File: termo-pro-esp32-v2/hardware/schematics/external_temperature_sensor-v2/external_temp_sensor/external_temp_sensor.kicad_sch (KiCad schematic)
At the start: 1 part

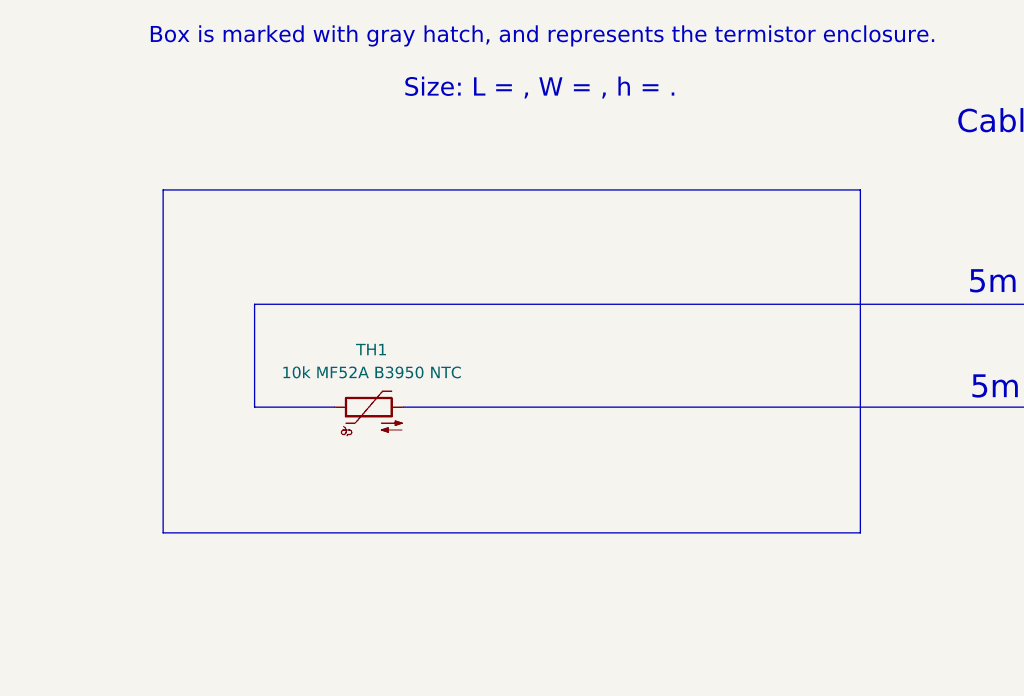
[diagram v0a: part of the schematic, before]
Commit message: Starting Unit PCB compleate.
Some footprint issues were encountered on the initial unit PCB, regarding the ceramic capacitors and the 1×02 5.08 mm screw terminal.

-In the thermostat schematic, the ceramic capacitors were updated to a disc footprint , as well in the starting unit scheme.

-Thermostat PCB is currently in progress.
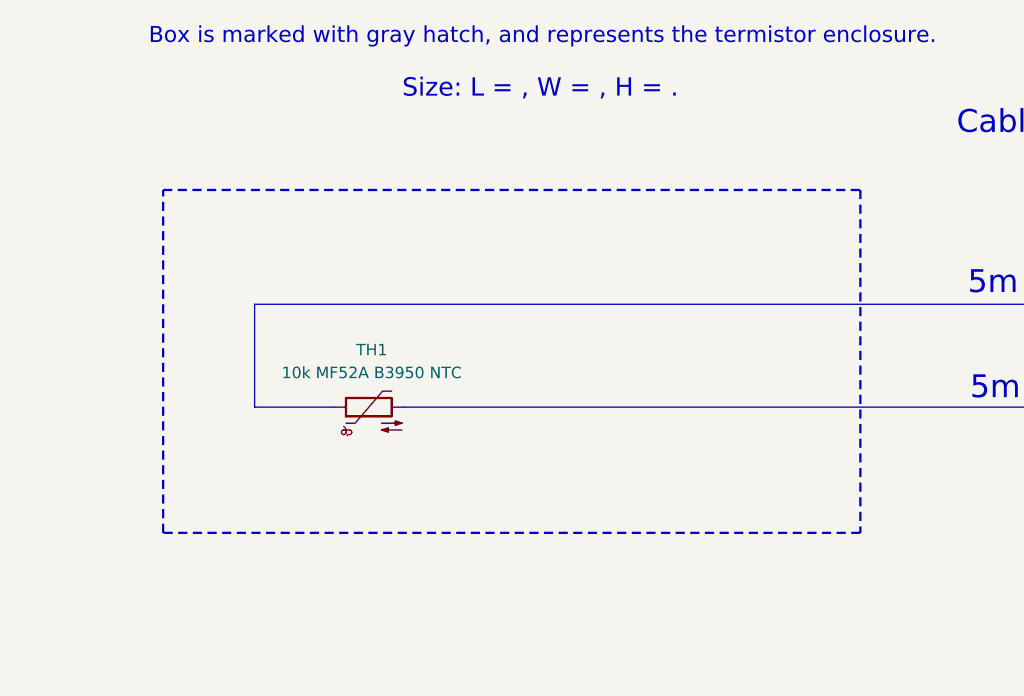
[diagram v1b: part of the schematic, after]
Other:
- note added: "Size: L = , W = , H = ."
- note removed: "Size: L = , W = , h = ."
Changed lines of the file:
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@@
 		(end 105.41 123.19)
 		(stroke
-			(width 0)
-			(type solid)
+			(width 0.254)
+			(type dash)
 			(color 0 255 0 1)
 		)
@@
 		)
 	)
-	(text "Size: L = , W = , h = . "
+	(text "Size: L = , W = , H = . "
 		(exclude_from_sim no)
 		(at 69.85 73.914 0)
